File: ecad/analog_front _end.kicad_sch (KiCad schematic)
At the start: 22 parts, among them J3 Red Banana Plug, J4 Black Banana Plug, SW3 SW_Push_DPDT, SW4 SW_SPST, U10 MCP3561, U3 OPA4388IDR, U7 LM4030-2.5

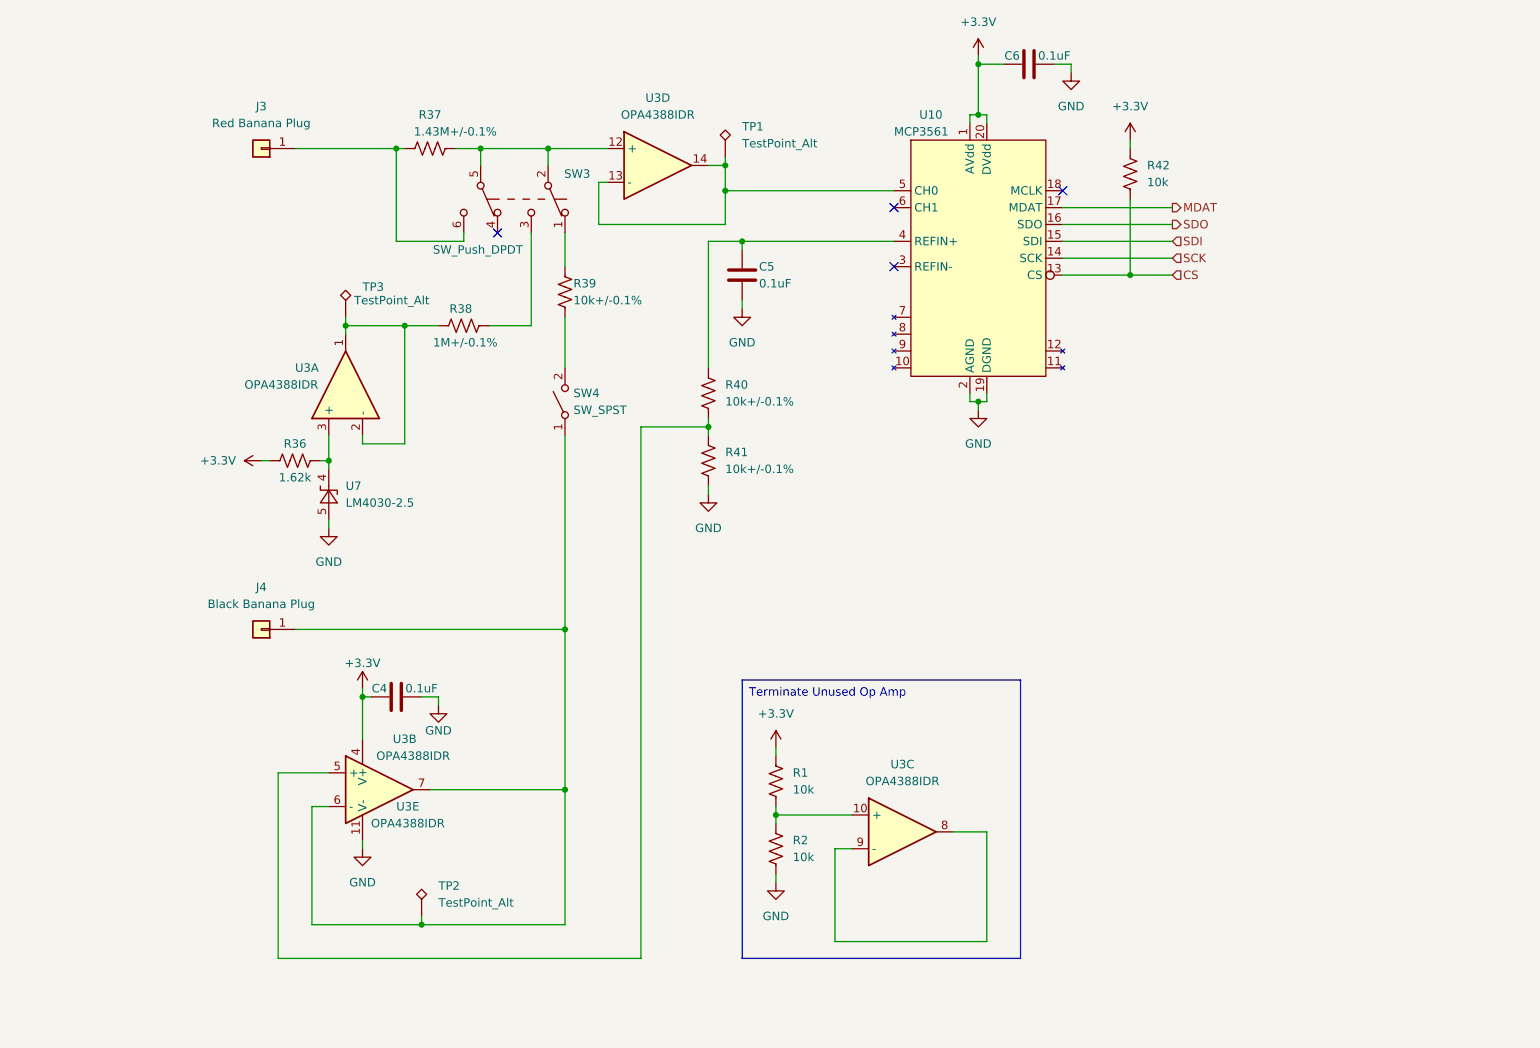
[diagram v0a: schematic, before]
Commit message: cap interpolation test
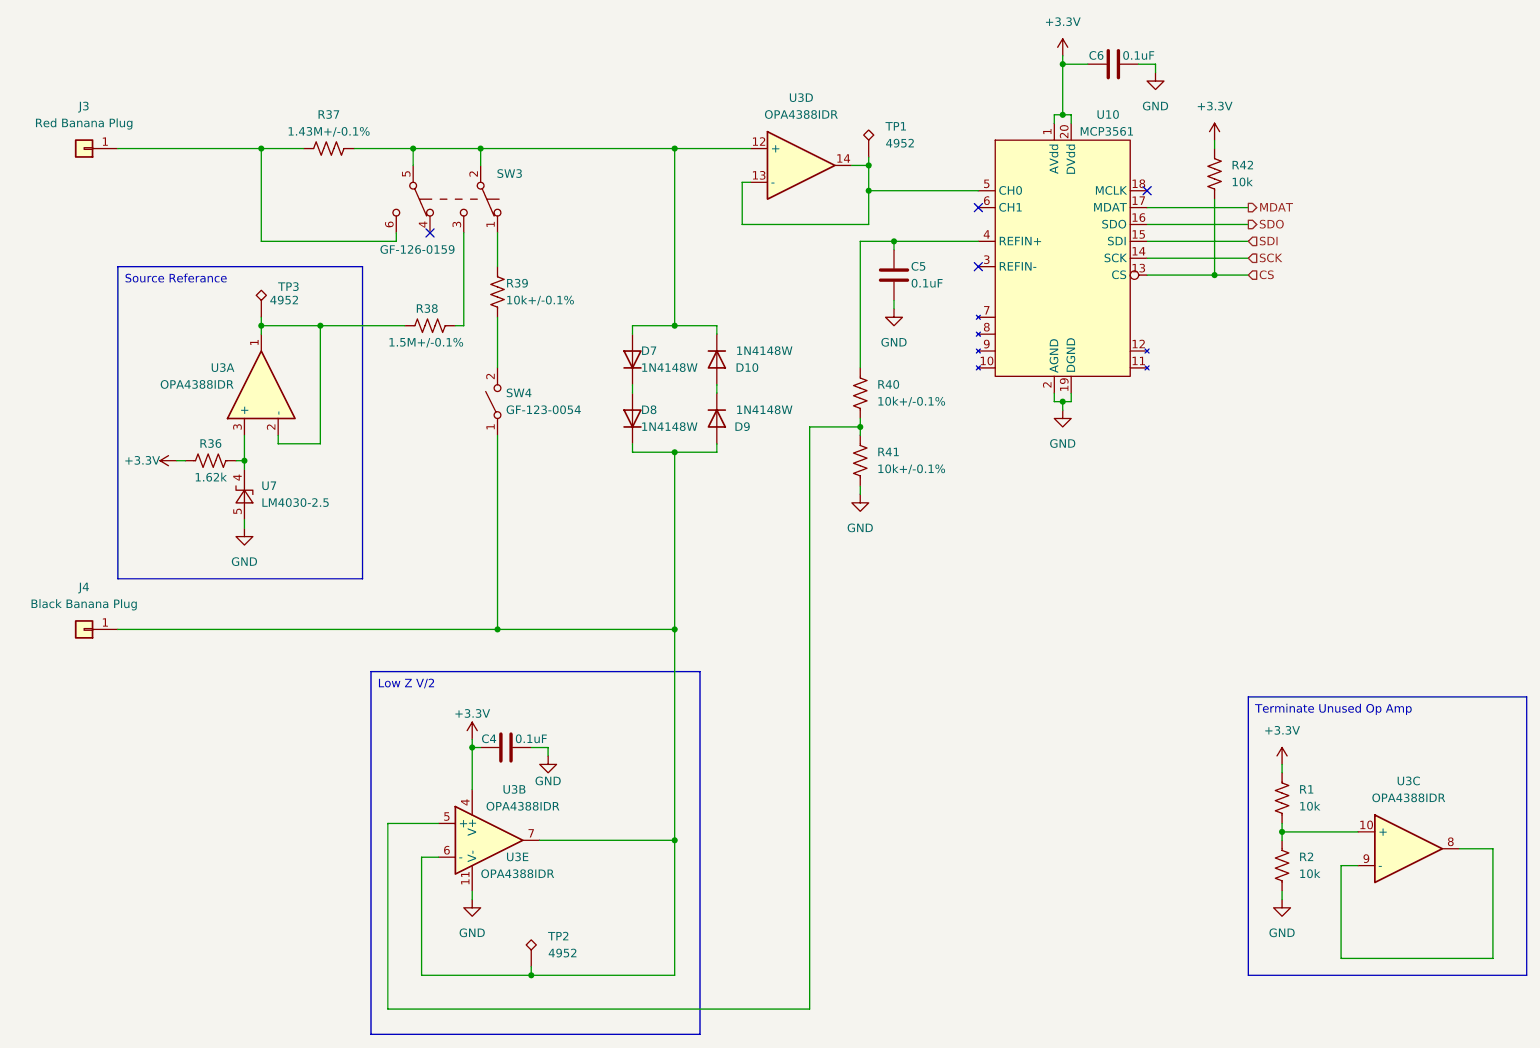
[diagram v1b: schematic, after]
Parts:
- added D10, D7, D8, D9: 1N4148W, Diode_SMD:D_SOD-123, symbol Diode:1N4148W
- R38: value 1M+/-0.1% -> 1.5M+/-0.1%
- SW3: value SW_Push_DPDT -> GF-126-0159; footprint (none) -> Multimeter:SW_GF-126-0159
- SW4: value SW_SPST -> GF-123-0054; footprint (none) -> Multimeter:SW_GF-123-0054
- TP1, TP2, TP3: value TestPoint_Alt -> 4952; footprint (none) -> TestPoint:TestPoint_THTPad_1.5x1.5mm_Drill0.7mm
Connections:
- net at J4.1 (Pin_1), SW4.1 (A), TP2.1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: now also D8.1 (K), D9.2 (A)
- net at R37.2, SW3.2 (B), SW3.5 (B)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: now also D10.1 (K), D7.2 (A)
- new net: D10.2 (A), D9.1 (K)
- new net: D7.1 (K), D8.2 (A)
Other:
- title: (none) -> Multimeter Analog Front End
- moved on the sheet: C4, C5, C6, J3, J4, R1, R2, R36, R37, R38, R39, R40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

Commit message: layout finished
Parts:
- removed D10, D7, D8, D9: 1N4148W, Diode_SMD:D_SOD-123, symbol Diode:1N4148W
- removed SW4: GF-123-0054, Multimeter:SW_GF-123-0054, symbol Switch:SW_SPST
- added JP1: ~, Jumper:SolderJumper-2_P1.3mm_Open_Pad1.0x1.5mm, symbol Jumper:SolderJumper_2_Open
- C4, C5, C6: Digikey Part # (none) -> 1276-1003-1-ND; Part # (none) -> CL21B104KBCNNNC; Unit Price (none) -> 0.1
- J3, J4: Digikey Part # (none) -> 36-575-8-ND; Part # (none) -> 575-8; Unit Price (none) -> 0.88
- R1, R2, R42: Digikey Part # (none) -> RMCF0805FT10K0CT-ND; Part # (none) -> RMCF0805FT10K0; Unit Price (none) -> 0.1
- R36: Digikey Part # (none) -> RMCF0805FT1K62CT-ND; Part # (none) -> RMCF0805FT1K62; Unit Price (none) -> 0.1
- R37: value 1.43M+/-0.1% -> 511k+/-0.1%; Digikey Part # (none) -> P511KDACT-ND; Part # (none) -> ERA-6AEB5113V
- R38: Digikey Part # (none) -> 408-2025-1-ND; Part # (none) -> RG2012P-155-B-T5; Unit Price (none) -> 0.1
- R39, R40, R41: Digikey Part # (none) -> P10KDACT-ND; Part # (none) -> ERA-6AEB103V; Unit Price (none) -> 0.32
- SW3: Digikey Part # (none) -> SW342-ND; Part # (none) -> GF-126-0159; Unit Price (none) -> 1.58
- TP1, TP2, TP3: Digikey Part # (none) -> 36-4952-ND; Part # (none) -> 4952; Unit Price (none) -> 0.26
- U10: Digikey Part # (none) -> 150-MCP3561RT-E/STCT-ND; Part # (none) -> MCP3561RT-E/ST; Unit Price (none) -> 3.00
- U3: Digikey Part # (none) -> 296-53511-1-ND; Part # (none) -> OPA4388IDR; Unit Price (none) -> 4.92
- U7: Digikey Part # (none) -> LM4030CMF-2.5/NOPBCT-ND; Part # (none) -> LM4030CMF-2.5/NOPB; Unit Price (none) -> 1.61
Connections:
- net at J4.1 (Pin_1), TP2.1, U3.6 (-)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: now also R39.2, JP1.1 (A)
- net at U10.6 (CH1): now also JP1.2 (B)
- no-connect marks 4 -> 3
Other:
- moved on the sheet: C4, C5, C6, J3, J4, R1, R2, R36, R37, R38, R39, R40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
